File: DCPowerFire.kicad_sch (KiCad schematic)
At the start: 49 parts, among them J1 Conn_01x01, J10 Conn_01x01, J11 Conn_01x01, J2 Conn_01x01, J3 USB_B_Micro, J4 Conn_01x01, J5 Conn_01x01, J6 Conn_02x03_Odd_Even, J7 Conn_01x01, J8 Conn_01x01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

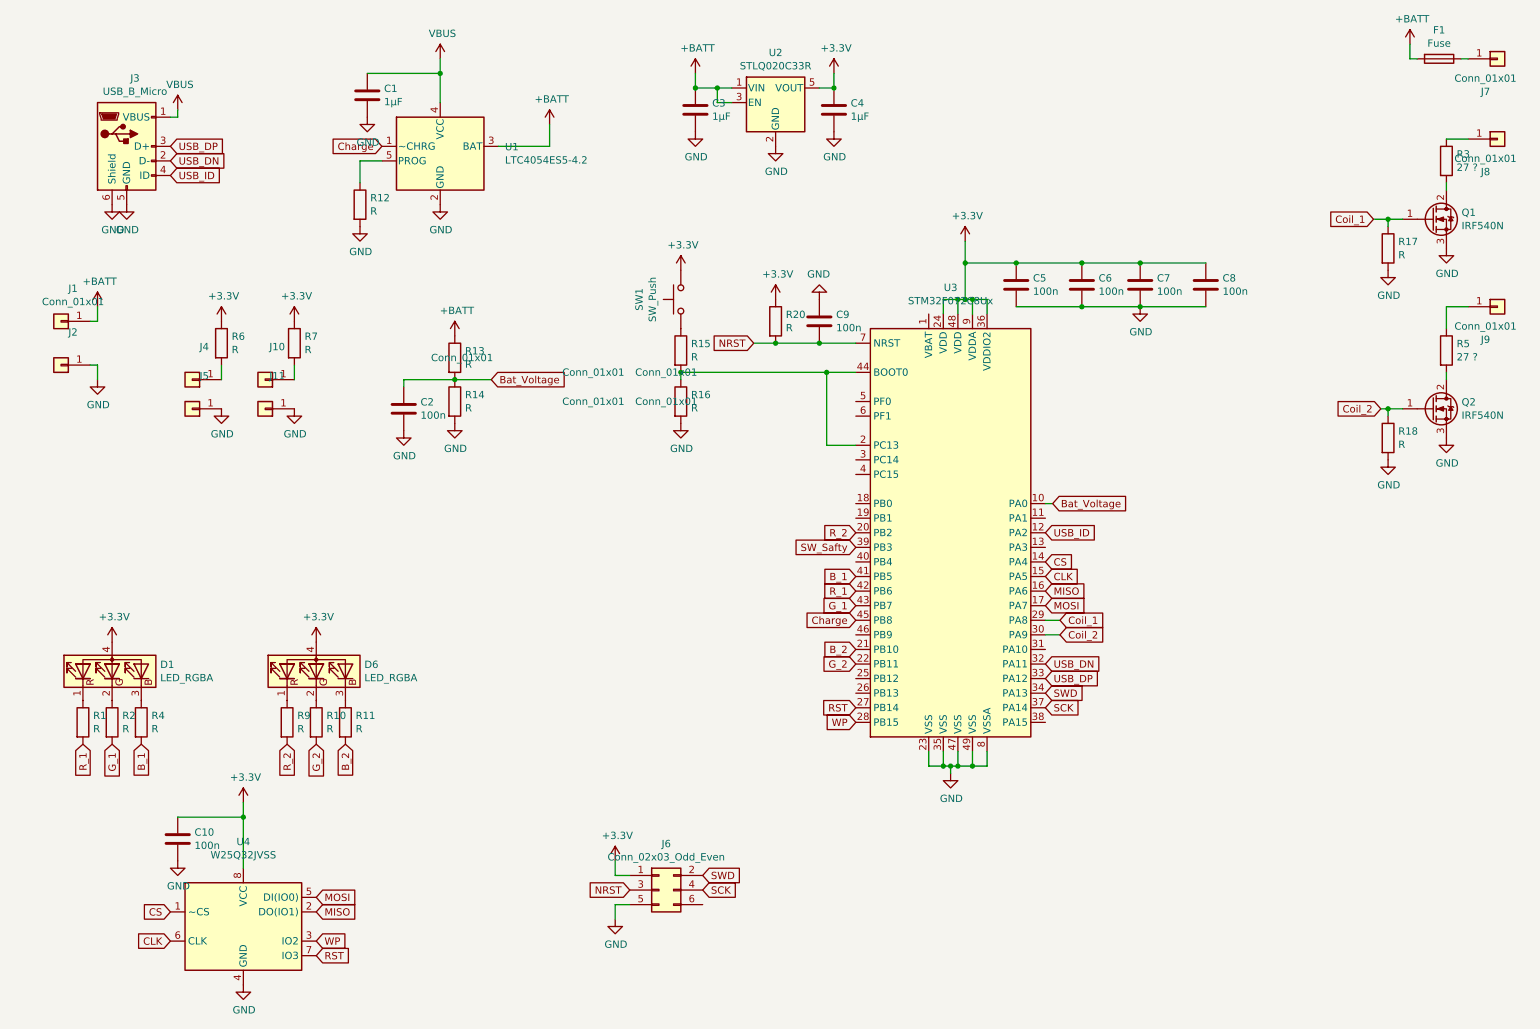
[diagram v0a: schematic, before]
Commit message: add missing NTC connections & begin silkscreen
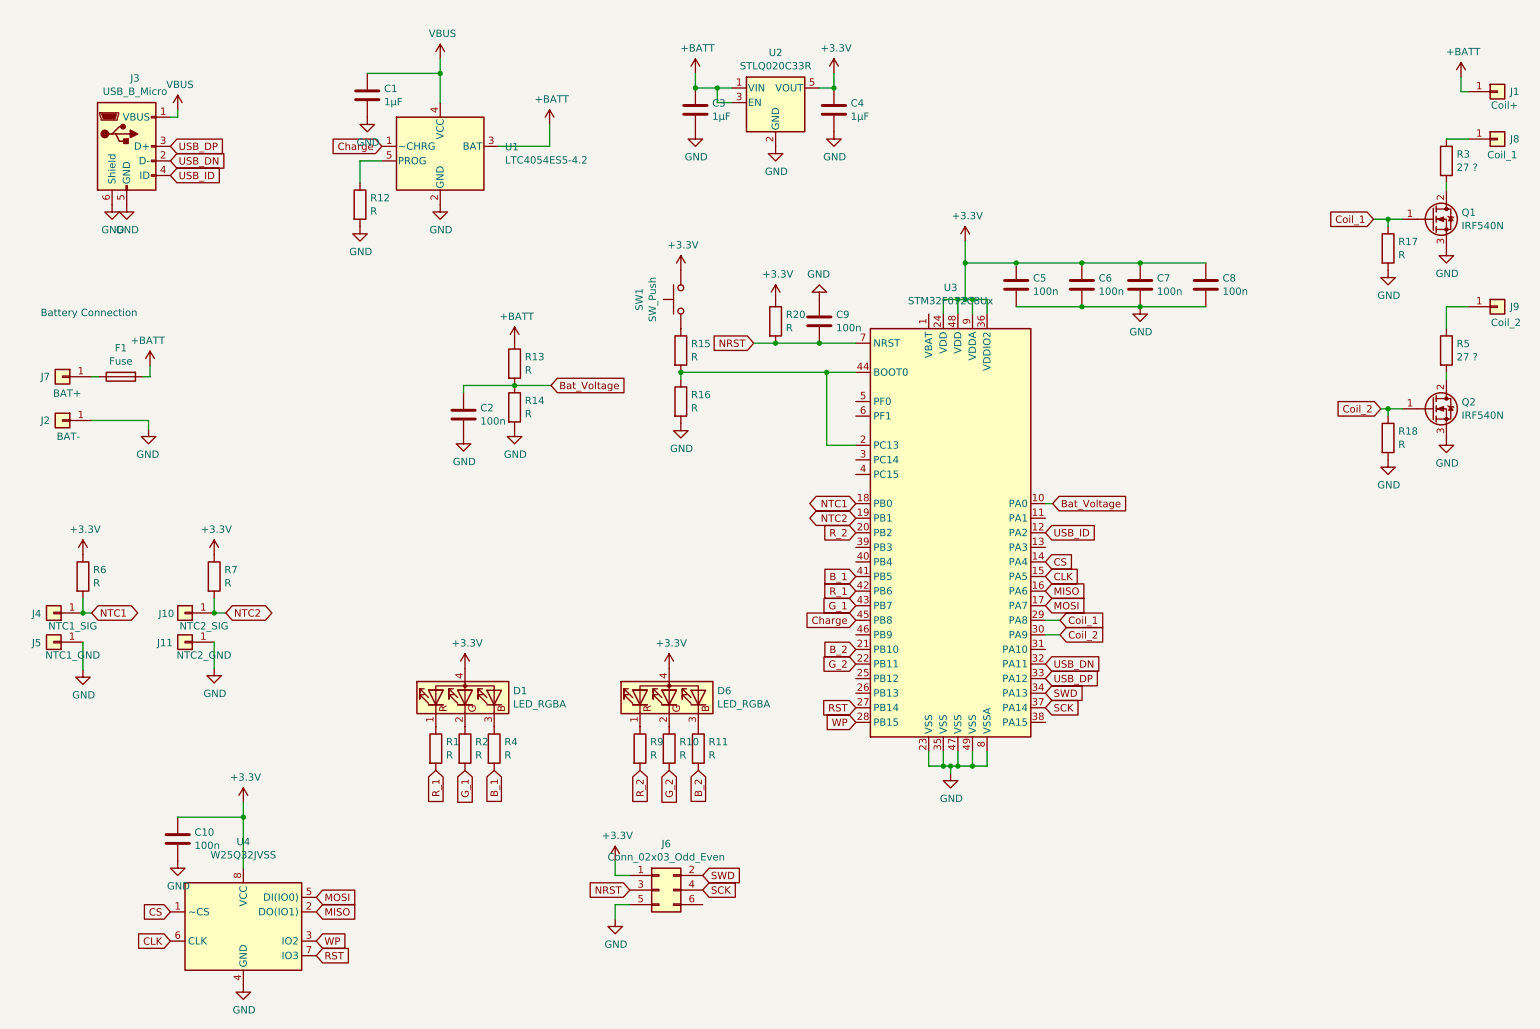
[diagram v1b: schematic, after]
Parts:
- J1: value Conn_01x01 -> Coil+; footprint TestPoint:TestPoint_Pad_1.0x1.0mm -> LeoDJ-kicad:TestPoint_Pad_1.0x1.0mm_NoSilk
- J10: value Conn_01x01 -> NTC2_SIG; footprint TestPoint:TestPoint_Pad_1.0x1.0mm -> LeoDJ-kicad:TestPoint_Pad_1.0x1.0mm_NoSilk
- J11: value Conn_01x01 -> NTC2_GND; footprint TestPoint:TestPoint_Pad_1.0x1.0mm -> LeoDJ-kicad:TestPoint_Pad_1.0x1.0mm_NoSilk
- J2: value Conn_01x01 -> BAT-; footprint TestPoint:TestPoint_Pad_1.0x1.0mm -> LeoDJ-kicad:TestPoint_Pad_1.0x1.0mm_NoSilk
- J4: value Conn_01x01 -> NTC1_SIG; footprint TestPoint:TestPoint_Pad_1.0x1.0mm -> LeoDJ-kicad:TestPoint_Pad_1.0x1.0mm_NoSilk
- J5: value Conn_01x01 -> NTC1_GND; footprint TestPoint:TestPoint_Pad_1.0x1.0mm -> LeoDJ-kicad:TestPoint_Pad_1.0x1.0mm_NoSilk
- J7: value Conn_01x01 -> BAT+; footprint TestPoint:TestPoint_Pad_1.0x1.0mm -> LeoDJ-kicad:TestPoint_Pad_1.0x1.0mm_NoSilk
- J8: value Conn_01x01 -> Coil_1; footprint TestPoint:TestPoint_Pad_1.0x1.0mm -> LeoDJ-kicad:TestPoint_Pad_1.0x1.0mm_NoSilk
- J9: value Conn_01x01 -> Coil_2; footprint TestPoint:TestPoint_Pad_1.0x1.0mm -> LeoDJ-kicad:TestPoint_Pad_1.0x1.0mm_NoSilk
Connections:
- net NTC1: now reaches J4.1 (Pin_1), R6.2
- net NTC1: now also U3.18 (PB0)
- net NTC2: now reaches J10.1 (Pin_1), R7.2
- net NTC2: now also U3.19 (PB1)
- net SW_Safty: no longer names the net of U3.39 (PB3)
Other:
- note added: "Battery Connection"
- moved on the sheet: C2, D1, D6, F1, J1, J10, J11, J2, J4, J5, J7, R1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

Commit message: add lid switch pads
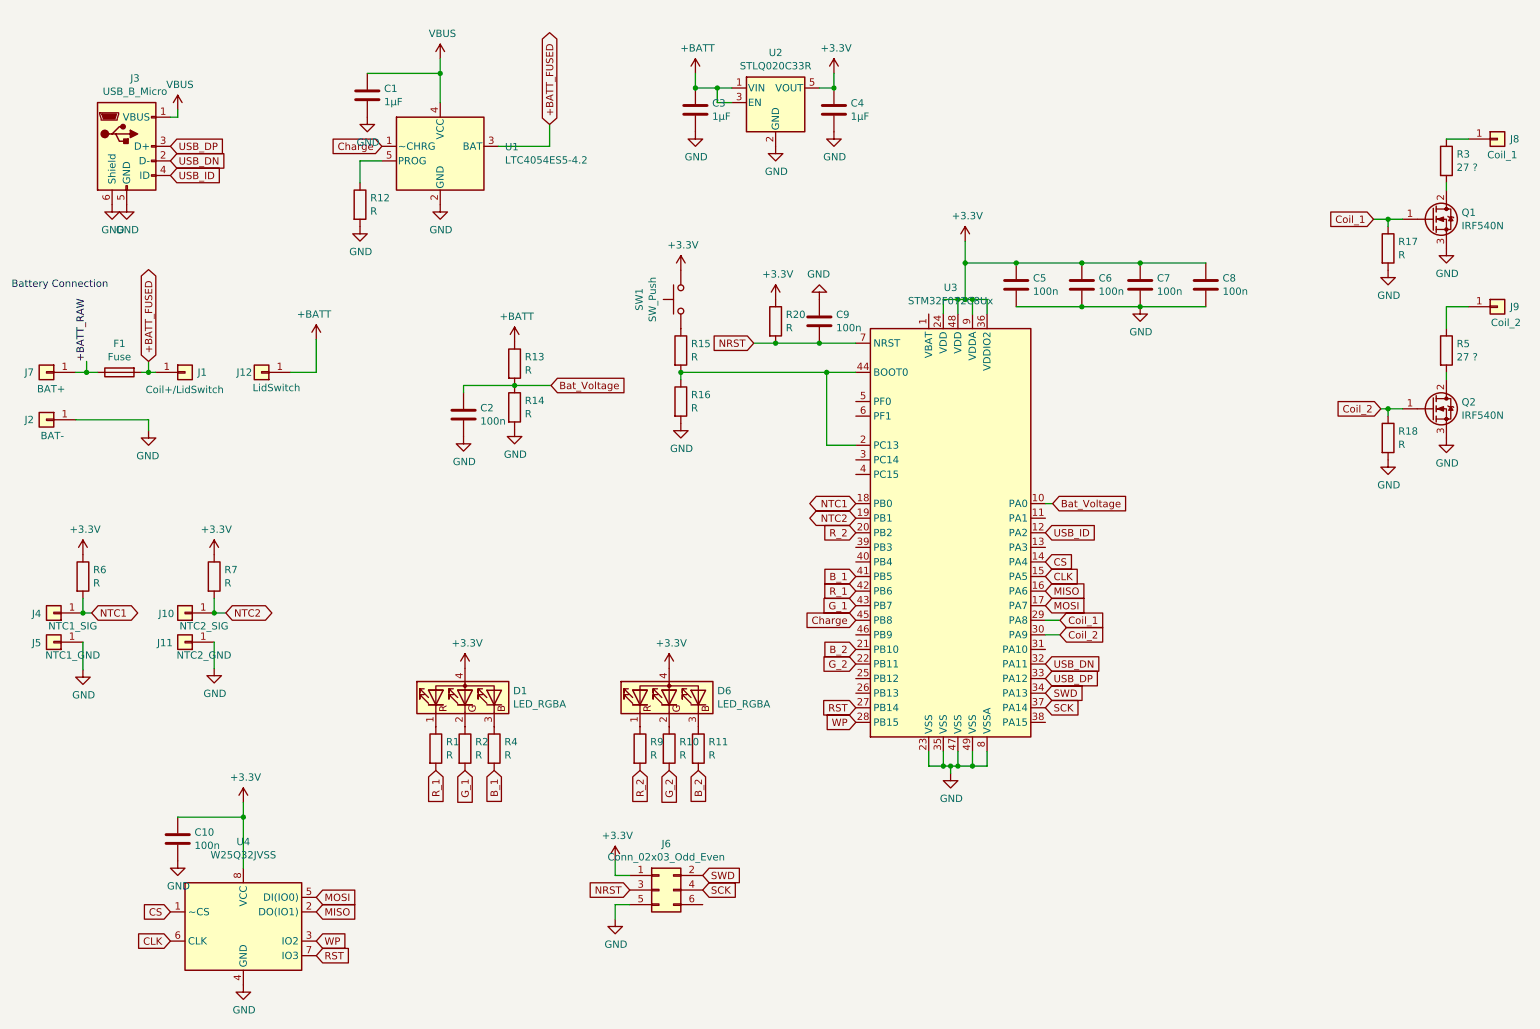
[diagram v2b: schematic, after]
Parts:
- added J12: LidSwitch, LeoDJ-kicad:TestPoint_Pad_1.0x1.0mm_NoSilk, symbol Connector_Generic:Conn_01x01
- J1: value Coil+ -> Coil+/LidSwitch
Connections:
- net +BATT: now also J12.1 (Pin_1); no longer F1.2, J1.1 (Pin_1), U1.3 (BAT)
- net +BATT_RAW: now reaches F1.1, J7.1 (Pin_1)
- new net +BATT_FUSED: F1.2, J1.1 (Pin_1), U1.3 (BAT)
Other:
- moved on the sheet: F1, J1, J2, J7

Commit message: minor fixes noticed during first assembly
resistor values, LED RGB mapping
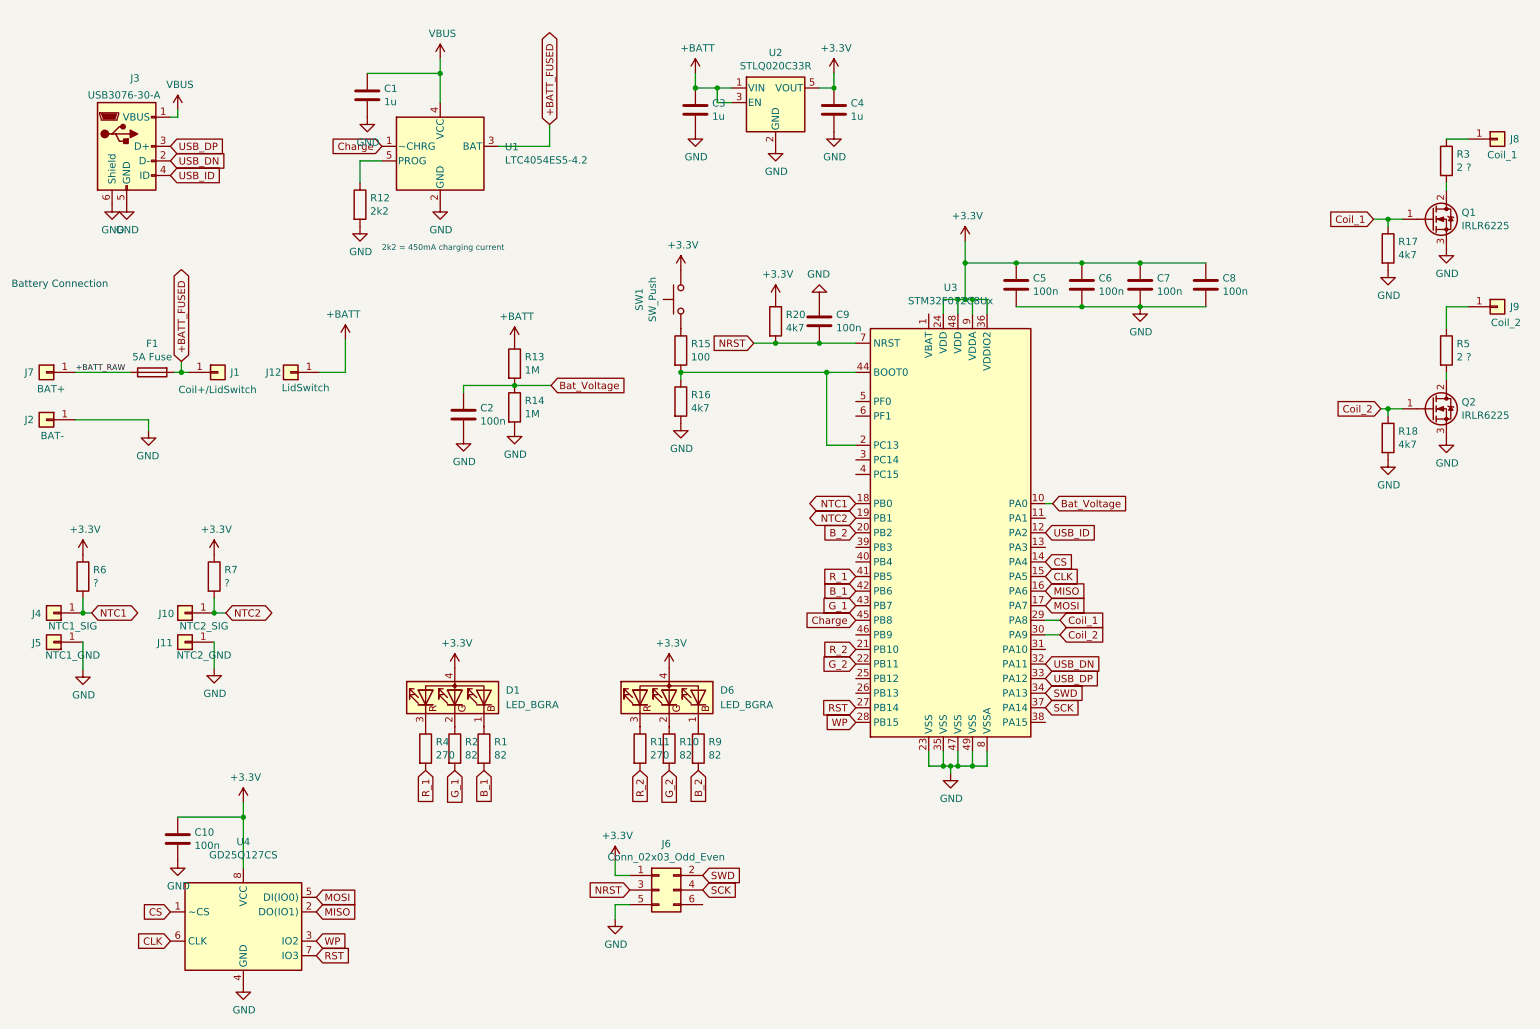
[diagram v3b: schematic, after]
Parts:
- removed D1, D6: LED_RGBA, Techbeard:RGB_0404, symbol Device:LED_RGBA
- added D1, D6: LED_BGRA, Techbeard:RGB_0404, symbol Device:LED_BGRA
- C1, C3, C4: value 1µF -> 1u
- F1: value Fuse -> 5A Fuse
- J3: value USB_B_Micro -> USB3076-30-A
- Q1, Q2: value IRF540N -> IRLR6225
- R1, R10, R2, R9: value R -> 82
- R11, R4: value R -> 270
- R12: value R -> 2k2
- R13, R14: value R -> 1M
- R15: value R -> 100
- R16, R17, R18, R20: value R -> 4k7
- R3, R5: value 27 ? -> 2 ?
- R6, R7: value R -> ?
- U4: value W25Q32JVSS -> GD25Q127CS
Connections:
- net +3V3: now also D1.4 (A), D6.4 (A)
- net B_1: now also R1.2, U3.42 (PB6); no longer R4.2, U3.41 (PB5)
- net B_2: now also R9.2, U3.20 (PB2); no longer R11.2, U3.21 (PB10)
- net R_1: now also R4.2, U3.41 (PB5); no longer R1.2, U3.42 (PB6)
- net R_2: now also R11.2, U3.21 (PB10); no longer R9.2, U3.20 (PB2)
- net at R1.1: now also D1.1 (BK)
- net at R2.1: now also D1.2 (GK)
- net at R4.1: now also D1.3 (RK)
- net at R9.1: now also D6.1 (BK)
- net at R10.1: now also D6.2 (GK)
- net at R11.1: now also D6.3 (RK)
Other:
- note added: "2k2 = 450mA charging current"
- moved on the sheet: F1, J1, J12, R1, R11, R2, R4, R9
